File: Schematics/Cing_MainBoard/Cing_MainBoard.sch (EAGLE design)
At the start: 85 parts, among them IC1 L293D, IC3 FT232RL, Q1 16mhz, U2 BMP180, U3 MPU-6050MPU6050

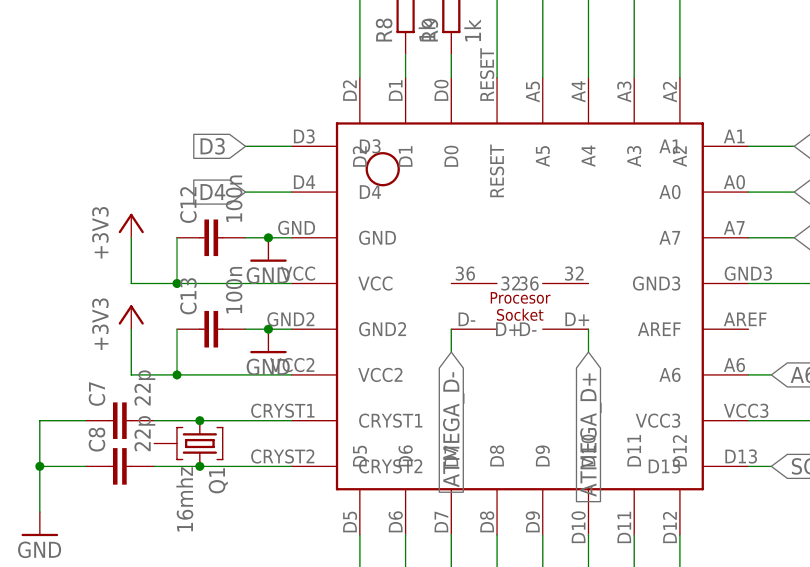
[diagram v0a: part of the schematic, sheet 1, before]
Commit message: Adding pin 36
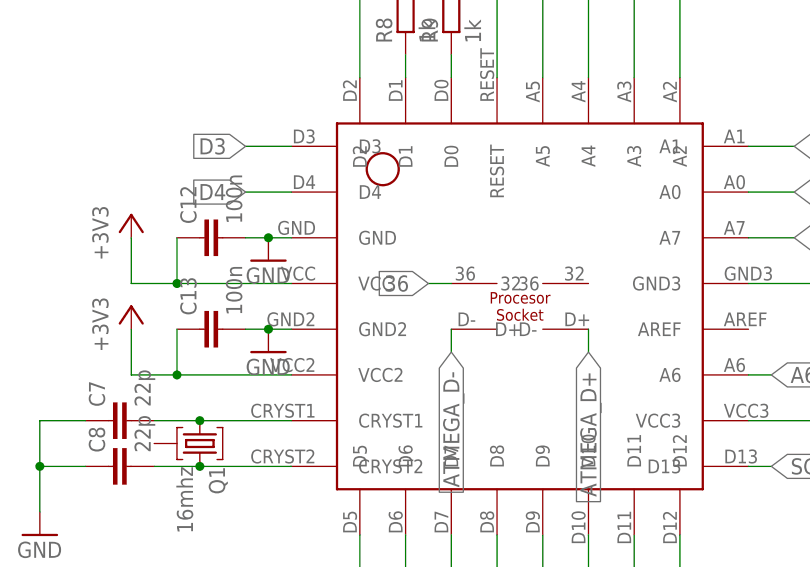
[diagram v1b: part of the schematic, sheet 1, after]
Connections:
- new net 36: U$1.36, U$2.+5V1
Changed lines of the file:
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@@
+</segment>
+</net>
+<net name="36" class="0">
+<segment>
+<pinref part="U$1" gate="G$1" pin="36"/>
+<wire x1="111.76" y1="106.68" x2="109.22" y2="106.68" width="0.1524" layer="91"/>
+<label x="109.22" y="106.68" size="1.778" layer="95" rot="R180" xref="yes"/>
 </segment>
 </net>
@@
 </segment>
 </net>
+<net name="36" class="0">
+<segment>
+<pinref part="U$2" gate="G$1" pin="+5V1"/>
+<wire x1="53.34" y1="17.78" x2="66.04" y2="17.78" width="0.1524" layer="91"/>
+<label x="66.04" y="17.78" size="1.778" layer="95" xref="yes"/>
+</segment>
+</net>

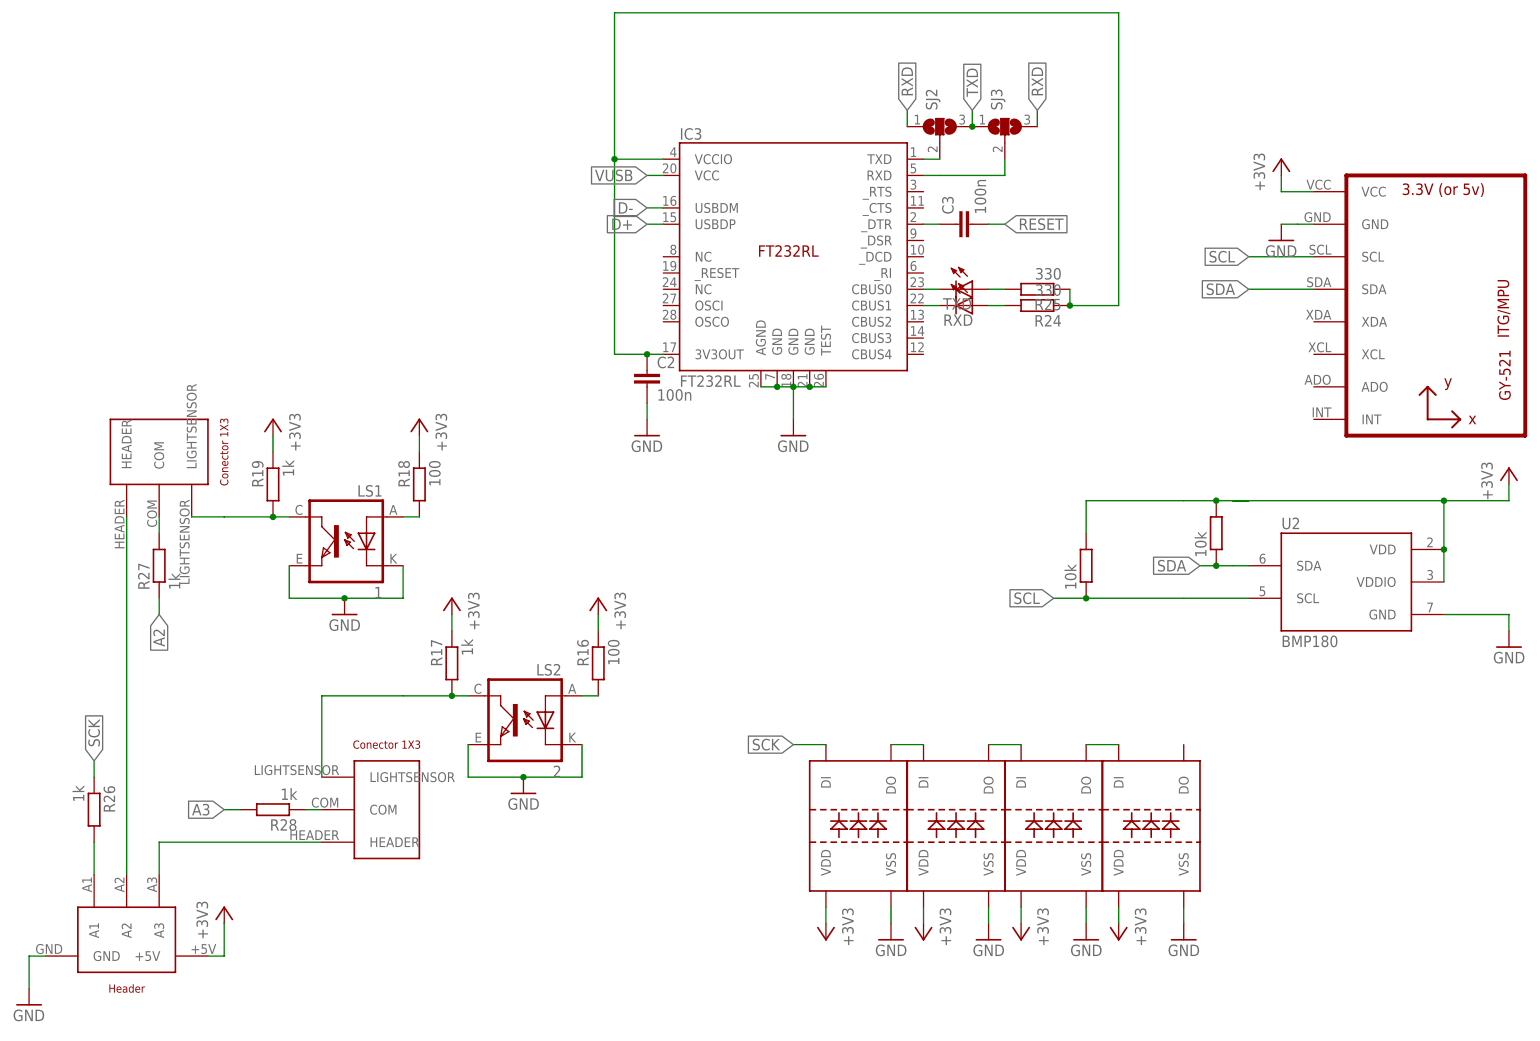
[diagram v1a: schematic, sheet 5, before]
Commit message: Adding optional 3V3 regulator
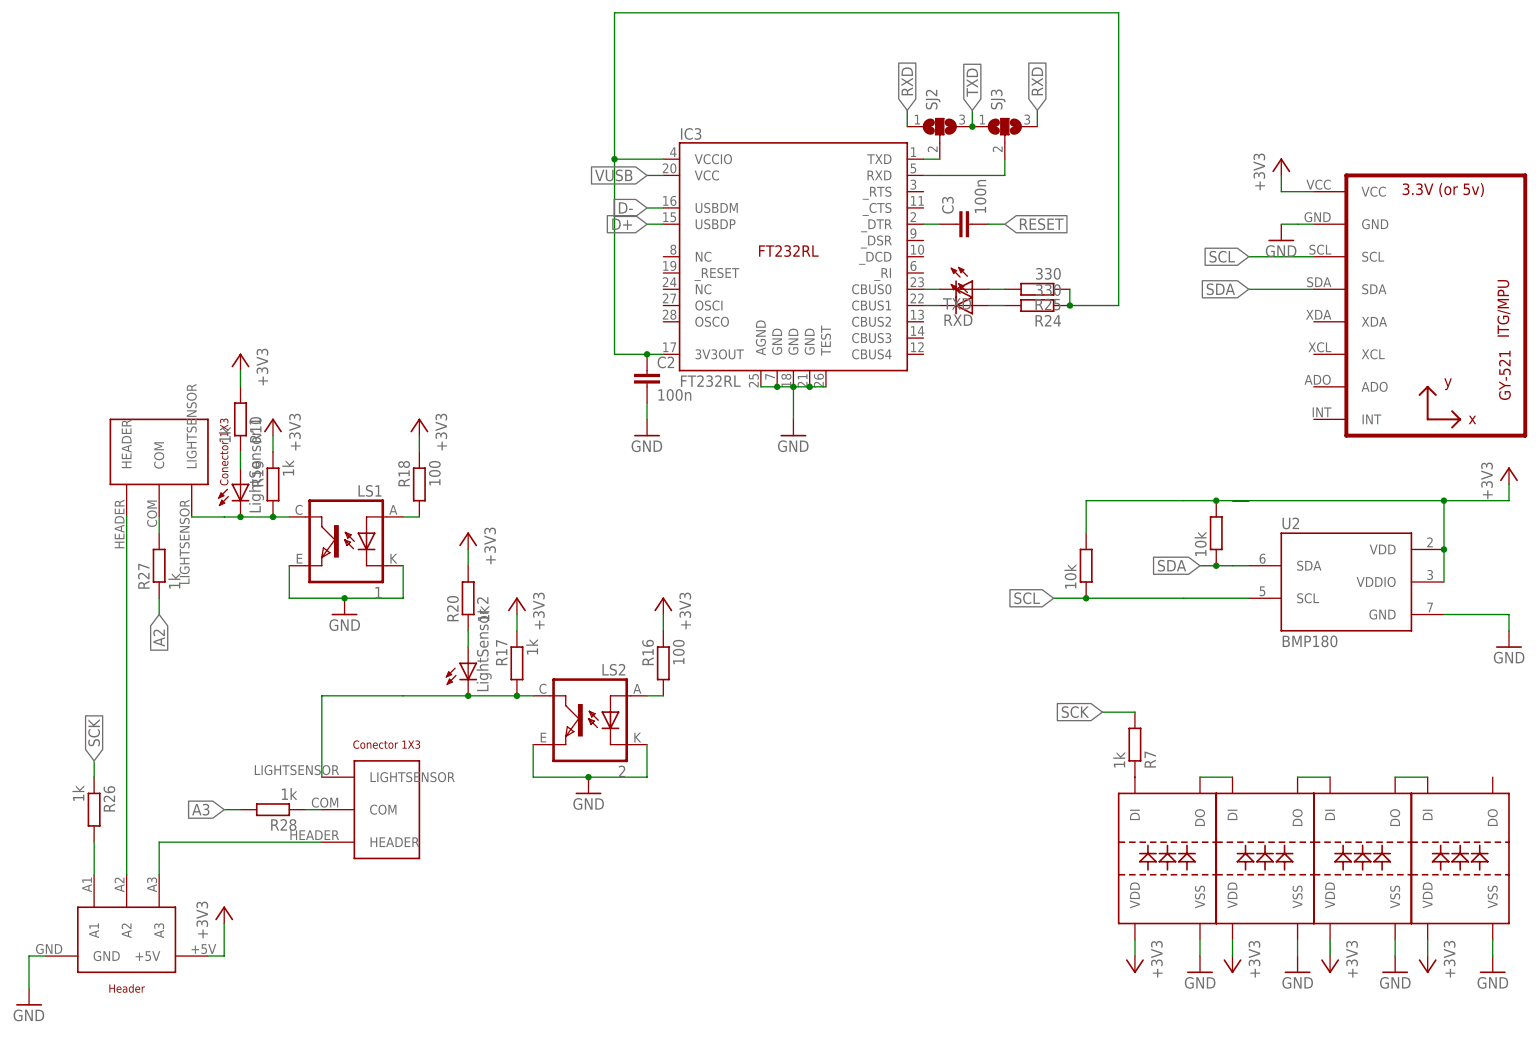
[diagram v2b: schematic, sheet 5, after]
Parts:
- added C4: 100uf, rcl:CPOL-EUE3.5-8
- added C5: 100n, rcl:C-EUC1206
- added IC2: LM1117T3.3-V, Cing Library:LM1117T3.3-V
- added R10, R20, R7: 1k, rcl:R-EU_R1206
- added TXD1: LightSensor 1, led:LEDSMT1206
- added TXD2: LightSensor 2, led:LEDSMT1206
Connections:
- new net N$12: LED5.DI, R7.1
- new net N$15: R10.1, TXD1.A
- new net N$17: R20.1, TXD2.A
- net +3V3: now also C4.+, C5.1, IC2.OUT, R10.2, R20.2
- net BAT+: now also IC2.IN
- net GND: now also C4.-, C5.2, IC2.GND
- net N$24: now also TXD1.C
- net N$45: now also TXD2.C
- net SCK: now also R7.2; no longer LED5.DI
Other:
- moved on the sheet: LS2, R16, R17
